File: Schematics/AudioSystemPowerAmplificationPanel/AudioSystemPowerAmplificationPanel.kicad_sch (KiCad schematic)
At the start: 10 parts, among them J1 AudioJack3, U1 TDA7294

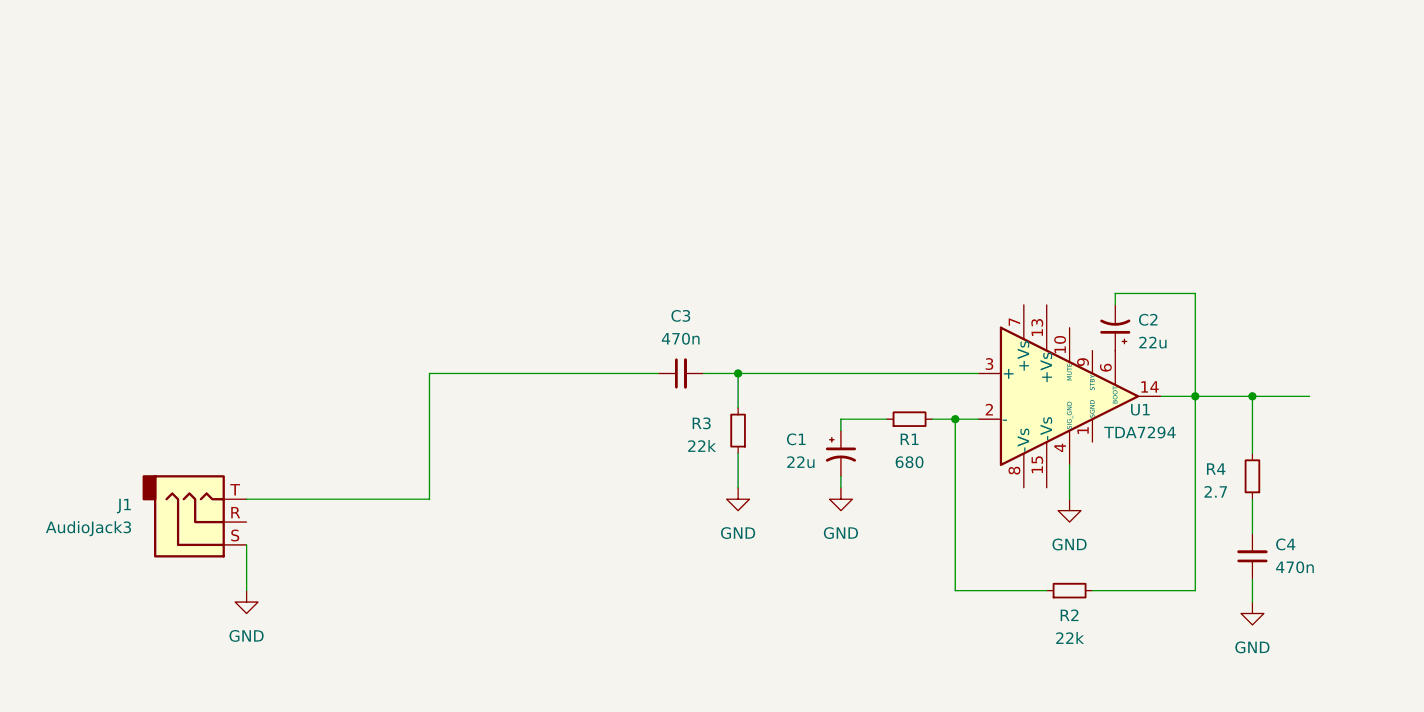
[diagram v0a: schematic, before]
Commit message: added full audio system schematic (not completed)
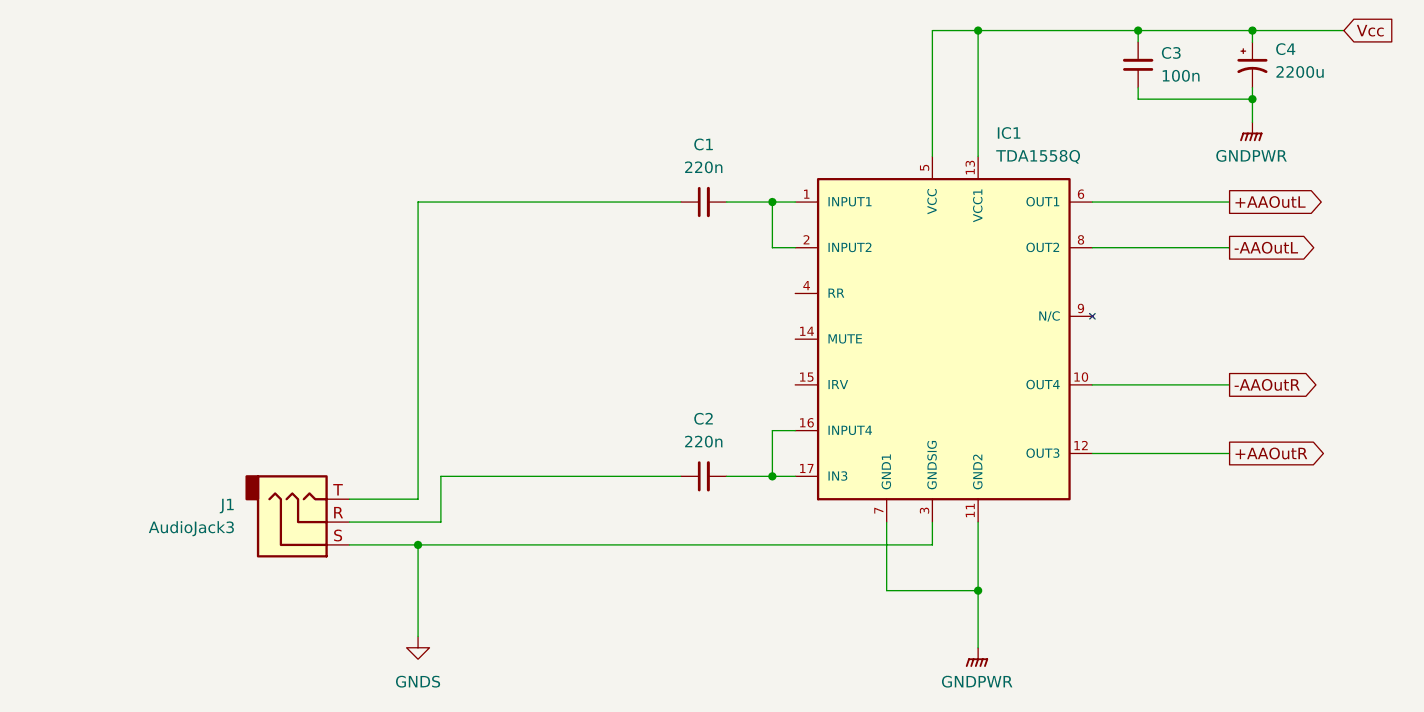
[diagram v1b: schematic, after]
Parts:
- removed C1, C2: 22u, symbol Device:C_Polarized_Small_US
- removed C4: 470n, symbol Device:C_Small
- removed R1: 680, symbol Device:R_Small
- removed R2, R3: 22k, symbol Device:R_Small
- removed R4: 2.7, symbol Device:R_Small
- removed U1: TDA7294, Package_TO_SOT_THT:TO-220-15_P2.54x2.54mm_StaggerOdd_Lead4.58mm_Vertical, symbol Amplifier_Audio:TDA7294
- added C1, C2: 220n, symbol Device:C_Small
- added C4: 2200u, symbol Device:C_Polarized_Small_US
- added IC1: TDA1558Q, AudioSystemFootprintLibrary:TDA1558Q, symbol AudioSystemSymbolLibrary:TDA1558Q
- C3: value 470n -> 100n
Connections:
- net Vcc: now reaches C3.2
- net Vcc: now also C4.1, IC1.13 (VCC1), IC1.5 (VCC)
- net at J1.R: now also C2.1
- net at J1.T: now also C1.1; no longer C3.1
- net GND renamed GNDS
- net GNDS: now also IC1.3 (GNDSIG)
- new net: C1.2, IC1.1 (INPUT1), IC1.2 (INPUT2)
- new net: C2.2, IC1.16 (INPUT4), IC1.17 (IN3)
- new net +AAOutL: IC1.6 (OUT1)
- new net +AAOutR: IC1.12 (OUT3)
- new net -AAOutL: IC1.8 (OUT2)
- new net -AAOutR: IC1.10 (OUT4)
- new net GNDPWR: C3.1, C4.2, IC1.11 (GND2), IC1.7 (GND1)
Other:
- moved on the sheet: J1
